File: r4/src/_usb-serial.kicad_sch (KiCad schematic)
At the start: 10 parts, among them U12 CP2102N-Axx-xQFN24

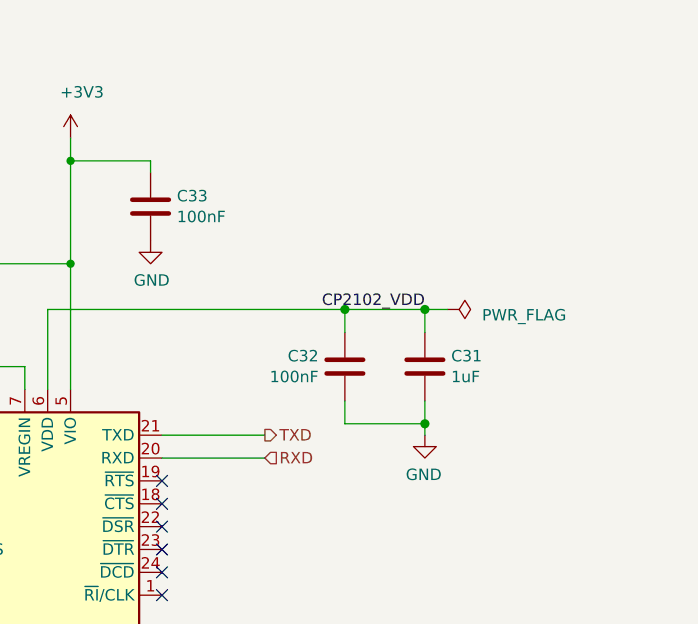
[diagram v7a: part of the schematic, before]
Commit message: Add cap to provide return AC current for the USB signals. On the return leg, the signals flow on the back (layer 6) so reference plane is directly underneath (layer 5). So to get the return current back to GND, an AC path is required from layer 5 (IN_VIN) to layer 2 (GND). C132 provides this
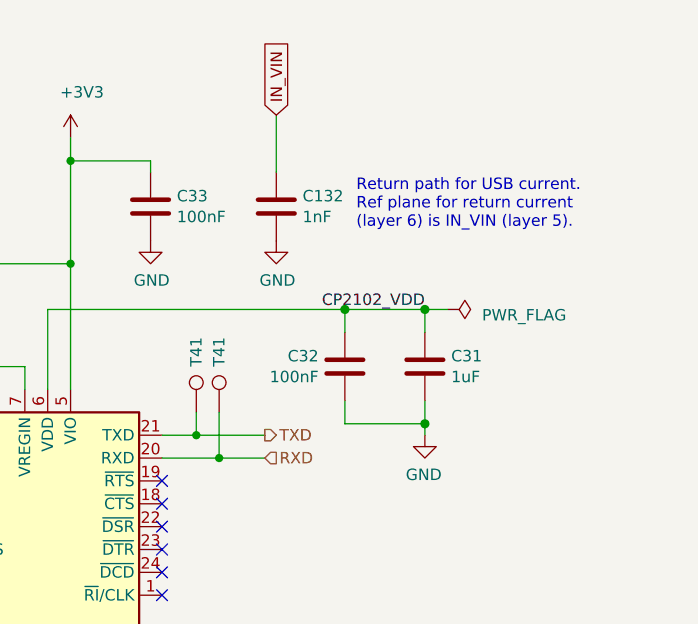
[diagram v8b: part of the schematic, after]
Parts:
- added C132: 1nF, Capacitor_SMD:C_0402_1005Metric, symbol Device:C
- added T41 (x2): (no value), TestPoint:TestPoint_Pad_D1.0mm, symbol Connector:TestPoint
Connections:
- net GND: now also C132.2
- net RXD: now also T41.1
- net TXD: now also T41.1
- new net IN_VIN: C132.1
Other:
- note added: "Return path for USB current. Ref plane for return current (layer 6) is IN_VIN (layer 5)."
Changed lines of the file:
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@@
   (junction (at 185.42 86.36) (diameter 1.016) (color 0 0 0 0)
   )
+  (junction (at 162.56 90.17) (diameter 0) (color 0 0 0 0)
+  )
   (junction (at 101.6 91.44) (diameter 1.016) (color 0 0 0 0)
   )
@@
   )
   (junction (at 120.65 100.33) (diameter 1.016) (color 0 0 0 0)
+  )
+  (junction (at 160.02 87.63) (diameter 0) (color 0 0 0 0)
   )
   (junction (at 110.49 81.28) (diameter 1.016) (color 0 0 0 0)
@@
     (stroke (width 0) (type solid))
   )
+  (wire (pts (xy 160.02 85.09) (xy 160.02 87.63))
+    (stroke (width 0) (type default))
+  )
   (wire (pts (xy 143.51 73.66) (xy 143.51 82.55))
     (stroke (width 0) (type solid))
@@
     (stroke (width 0) (type solid))
   )
+  (wire (pts (xy 162.56 85.09) (xy 162.56 90.17))
+    (stroke (width 0) (type default))
+  )
+  (wire (pts (xy 168.91 52.07) (xy 168.91 58.42))
+    (stroke (width 0) (type default))
+  )
   (wire (pts (xy 146.05 54.61) (xy 146.05 57.15))
     (stroke (width 0) (type solid))
   )
-  (wire (pts (xy 156.21 90.17) (xy 167.64 90.17))
+  (wire (pts (xy 156.21 90.17) (xy 162.56 90.17))
+    (stroke (width 0) (type solid))
+  )
+  (wire (pts (xy 160.02 87.63) (xy 167.64 87.63))
     (stroke (width 0) (type solid))
   )
@@
     (stroke (width 0) (type solid))
   )
-  (wire (pts (xy 156.21 87.63) (xy 167.64 87.63))
+  (wire (pts (xy 156.21 87.63) (xy 160.02 87.63))
     (stroke (width 0) (type solid))
   )
@@
     (stroke (width 0) (type solid))
   )
+  (wire (pts (xy 162.56 90.17) (xy 167.64 90.17))
+    (stroke (width 0) (type solid))
+  )
   (wire (pts (xy 154.94 58.42) (xy 154.94 57.15))
     (stroke (width 0) (type solid))
@@
   (wire (pts (xy 110.49 91.44) (xy 101.6 91.44))
     (stroke (width 0) (type solid))
+  )
+  (text "Return path for USB current.\nRef plane for return current \n(layer 6) is IN_VIN (layer 5)."
+    (at 177.8 64.77 0)
+    (effects (font (size 1.27 1.27)) (justify left bottom))
   )
   (text "Bus powered configuration" (at 127.635 60.96 0)
@@
     (effects (font (size 1.27 1.27)) (justify right bottom))
   )
+  (global_label "IN_VIN" (shape input) (at 168.91 52.07 90) (fields_autoplaced)
+    (effects (font (size 1.27 1.27)) (justify left))
+    (property "Intersheetrefs" "${INTERSHEET_REFS}" (at 168.91 43.3011 90)
+      (effects (font (size 1.27 1.27)) (justify left) hide)
+    )
+  )
   (hierarchical_label "USB_DP" (shape bidirectional) (at 110.49 105.41 180) (fields_autoplaced)
     (effects (font (size 1.27 1.27)) (justify right))
@@
     )
   )
+  (symbol (lib_id "Device:C") (at 168.91 62.23 0) (unit 1)
+    (in_bom yes) (on_board yes) (dnp no)
+    (property "Reference" "C132" (at 171.831 61.0616 0)
+      (effects (font (size 1.27 1.27)) (justify left))
+    )
+    (property "Value" "1nF" (at 171.831 63.373 0)
+      (effects (font (size 1.27 1.27)) (justify left))
+    )
+    (property "Footprint" "Capacitor_SMD:C_0402_1005Metric" (at 169.8752 66.04 0)
+      (effects (font (size 1.27 1.27)) hide)
+    )
+    (property "Datasheet" "~" (at 168.91 62.23 0)
+      (effects (font (size 1.27 1.27)) hide)
+    )
+    (pin "1")
+    (pin "2")
+    (instances
+      (project "bugg-main-r4"
+        (path "/e3eb514f-6ce4-4abe-ba20-f82f0015628f/26331aa8-35b7-4c22-8a42-89230ada1085"
+          (reference "C132") (unit 1) (value "1nF") (footprint "Capacitor_SMD:C_0402_1005Metric")
+        )
+      )
+    )
+  )
   (symbol (lib_id "Device:C") (at 101.6 86.36 0) (mirror y) (unit 1)
     (in_bom yes) (on_board yes) (dnp no)
@@
     )
   )
+  (symbol (lib_id "power:GND") (at 168.91 66.04 0) (unit 1)
+    (in_bom yes) (on_board yes) (dnp no)
+    (property "Reference" "#PWR0327" (at 168.91 72.39 0)
+      (effects (font (size 1.27 1.27)) hide)
+    )
+    (property "Value" "GND" (at 169.037 70.4342 0)
+      (effects (font (size 1.27 1.27)))
+    )
+    (property "Footprint" "" (at 168.91 66.04 0)
+      (effects (font (size 1.27 1.27)) hide)
+    )
+    (property "Datasheet" "" (at 168.91 66.04 0)
+      (effects (font (size 1.27 1.27)) hide)
+    )
+    (pin "1")
+    (instances
+      (project "bugg-main-r4"
+        (path "/e3eb514f-6ce4-4abe-ba20-f82f0015628f/26331aa8-35b7-4c22-8a42-89230ada1085"
+          (reference "#PWR0327") (unit 1) (value "GND") (footprint "")
+        )
+      )
+    )
+  )
   (symbol (lib_id "power:GND") (at 185.42 87.63 0) (mirror y) (unit 1)
     (in_bom yes) (on_board yes) (dnp no)
@@
         (path "/e3eb514f-6ce4-4abe-ba20-f82f0015628f/26331aa8-35b7-4c22-8a42-89230ada1085"
           (reference "C40") (unit 1) (value "1uF") (footprint "Capacitor_SMD:C_0402_1005Metric")
+        )
+      )
+    )
+  )
+  (symbol (lib_id "Connector:TestPoint") (at 160.02 85.09 0) (unit 1)
+    (in_bom yes) (on_board yes) (dnp no)
+    (property "Reference" "T41" (at 160.02 80.01 90)
+      (effects (font (size 1.27 1.27)) (justify left))
+    )
+    (property "Value" " " (at 161.29 80.01 90)
+      (effects (font (size 1.27 1.27)) (justify left))
+    )
+    (property "Footprint" "TestPoint:TestPoint_Pad_D1.0mm" (at 165.1 85.09 0)
+      (effects (font (size 1.27 1.27)) hide)
+    )
+    (property "Datasheet" "~" (at 165.1 85.09 0)
+      (effects (font (size 1.27 1.27)) hide)
+    )
+    (pin "1")
+    (instances
+      (project "bugg-main-r4"
+        (path "/e3eb514f-6ce4-4abe-ba20-f82f0015628f/e93db74d-0429-4e7f-b256-c16b4c3a83e7"
+          (reference "T41") (unit 1) (value " ") (footprint "TestPoint:TestPoint_Pad_D1.0mm")
+        )
+        (path "/e3eb514f-6ce4-4abe-ba20-f82f0015628f/26331aa8-35b7-4c22-8a42-89230ada1085"
+          (reference "T53") (unit 1) (value " ") (footprint "TestPoint:TestPoint_Pad_D1.0mm")
         )
       )
@@
         )
       )
+    )
+  )
+  (symbol (lib_id "Connector:TestPoint") (at 162.56 85.09 0) (unit 1)
+    (in_bom yes) (on_board yes) (dnp no)
+    (property "Reference" "T41" (at 162.56 80.01 90)
+      (effects (font (size 1.27 1.27)) (justify left))
+    )
+    (property "Value" " " (at 163.83 80.01 90)
+      (effects (font (size 1.27 1.27)) (justify left))
+    )
+    (property "Footprint" "TestPoint:TestPoint_Pad_D1.0mm" (at 167.64 85.09 0)
+      (effects (font (size 1.27 1.27)) hide)
+    )
+    (property "Datasheet" "~" (at 167.64 85.09 0)
+      (effects (font (size 1.27 1.27)) hide)
+    )
+    (pin "1")
+    (instances
+      (project "bugg-main-r4"
+        (path "/e3eb514f-6ce4-4abe-ba20-f82f0015628f/e93db74d-0429-4e7f-b256-c16b4c3a83e7"
+          (reference "T41") (unit 1) (value " ") (footprint "TestPoint:TestPoint_Pad_D1.0mm")
+        )
+        (path "/e3eb514f-6ce4-4abe-ba20-f82f0015628f/26331aa8-35b7-4c22-8a42-89230ada1085"
+          (reference "T54") (unit 1) (value " ") (footprint "TestPoint:TestPoint_Pad_D1.0mm")
+        )
+      )
